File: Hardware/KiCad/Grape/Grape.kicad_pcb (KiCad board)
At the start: 2 copper layers, 68.6 x 53.3 mm, 85 parts, among them J1 USB_MICROB, J19 POWER_JACKPTH, J3 ARDUINO_R3, P1 CONN_01X03, P10 CONN_01X03, P11 CONN_01X03, P12 CONN_01X03, P13 CONN_01X03, P14 CONN_01X03, P15 CONN_01X03, P16 CONN_01X03, P17 CONN_01X03, P18 CONN_01X03, P19 CONN_01X03, P2 CONN_01X03, P20 CONN_01X03, P21 CONN_01X03, P22 CONN_01X03, P23 I2C, P3 CONN_01X03, P4 CONN_01X03, P5 CONN_01X03, P6 CONN_01X03, P7 CONN_01X03, P8 CONN_01X03, P9 CONN_01X03, Q1 2N7002PW, Q4 FDN340P, Q5 FDN340P, SW1 SW_SPDT, U1 FT231XS, U2 LM358, U3 AMS1117-3.3, U4 ATMEGA328P_TQFP, U8 MP2307SO, Y1 16MHz

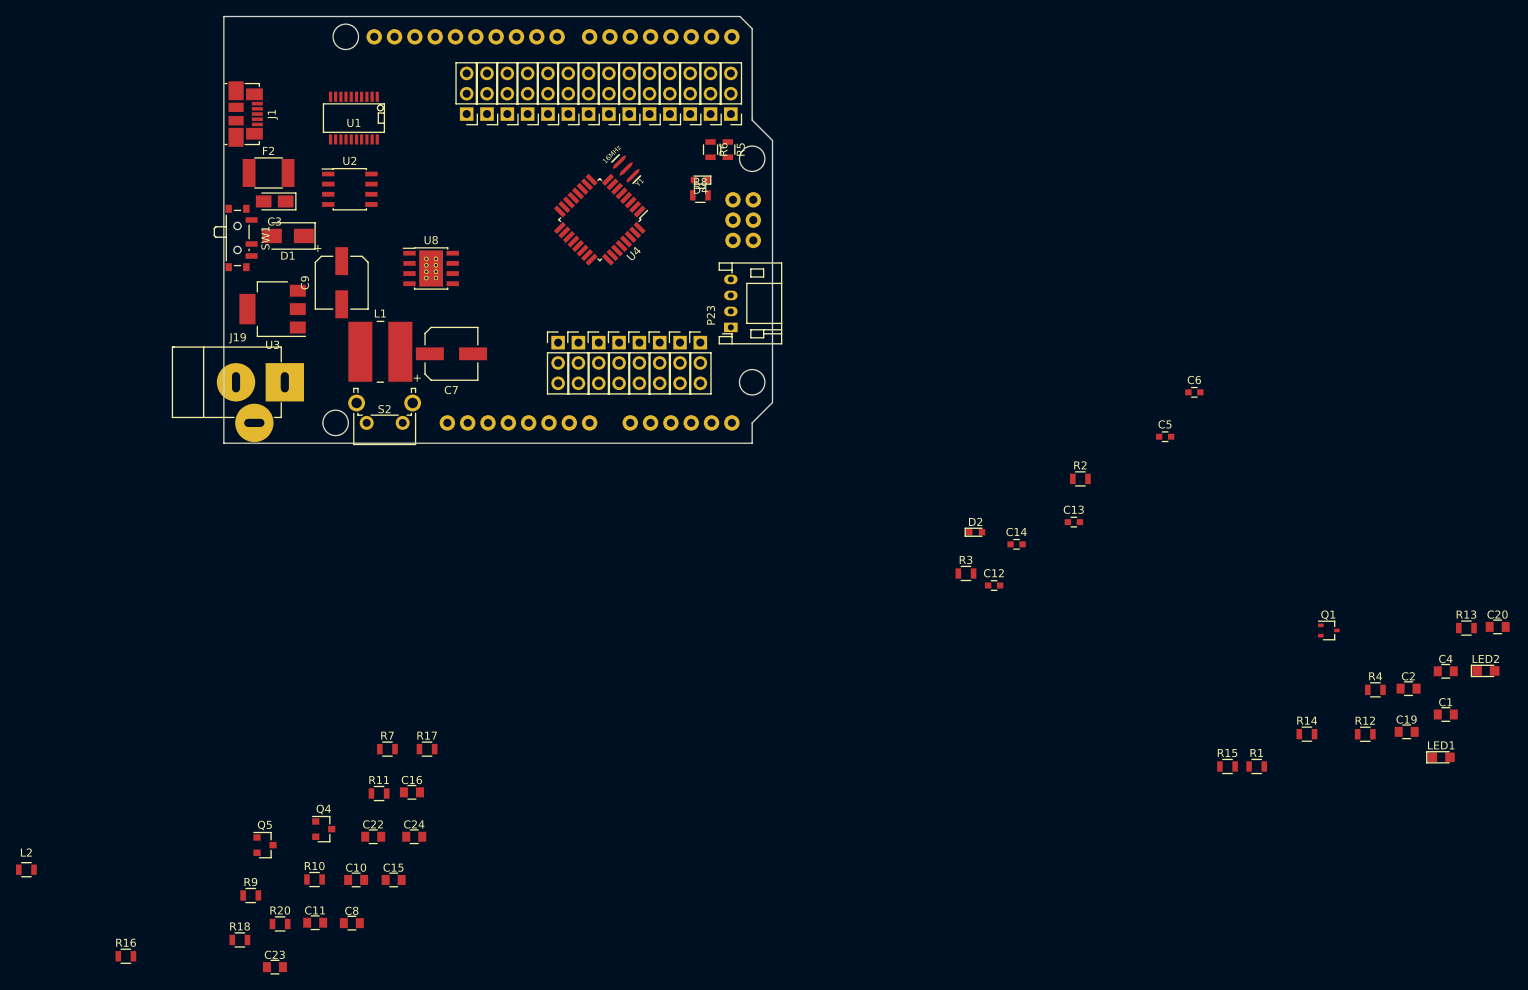
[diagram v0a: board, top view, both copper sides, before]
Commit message: 3D terminado
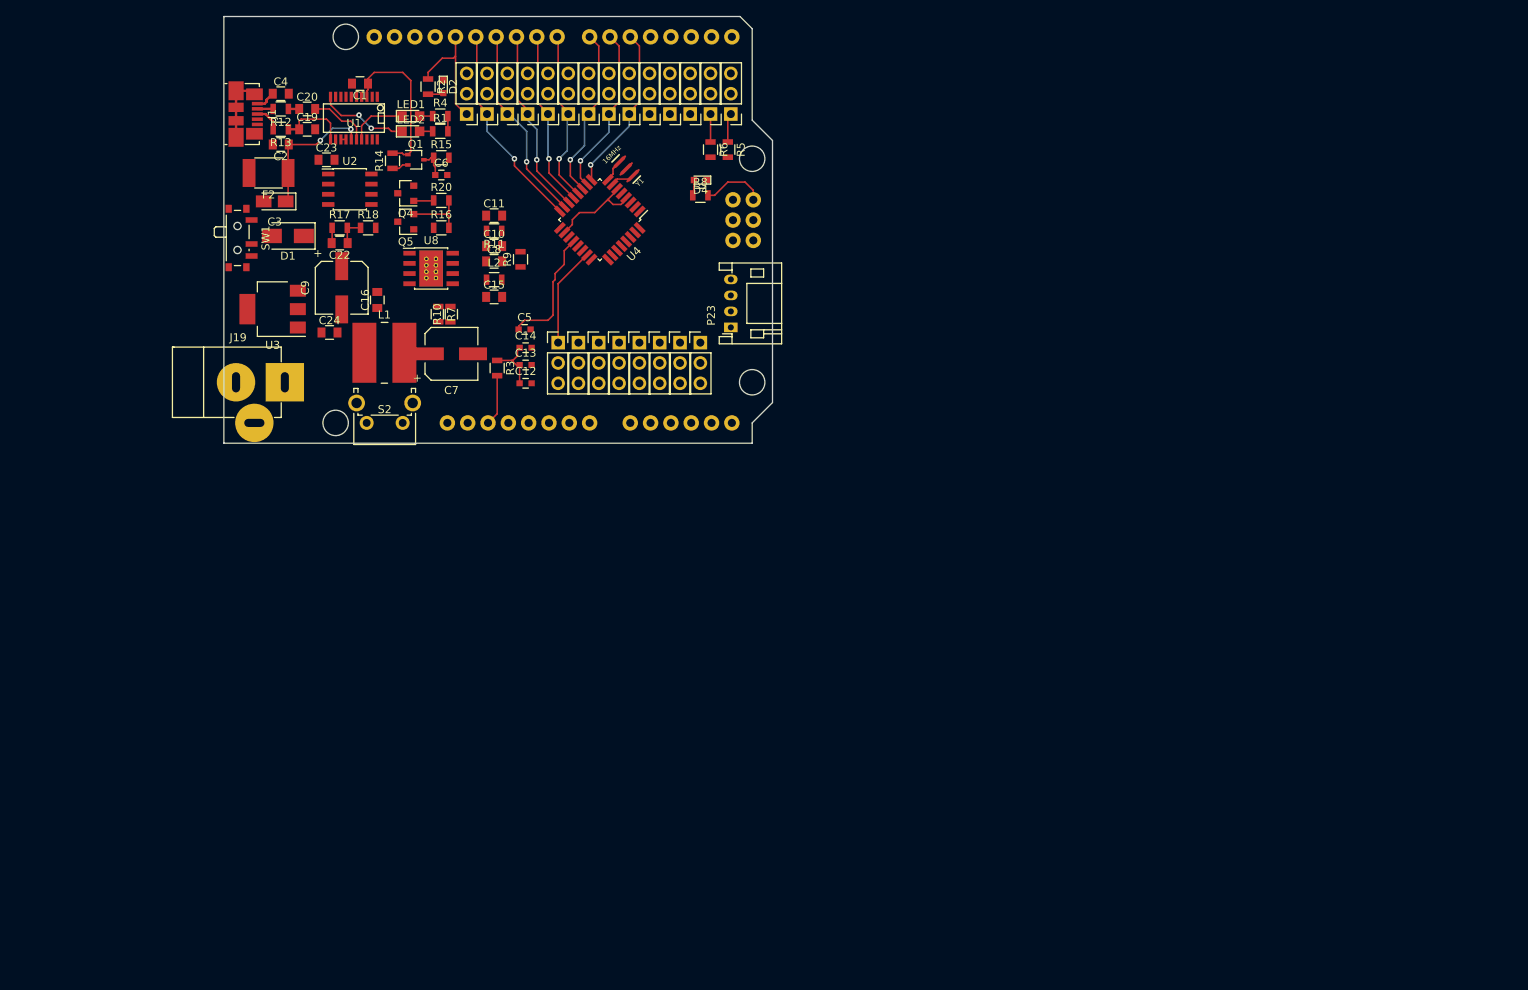
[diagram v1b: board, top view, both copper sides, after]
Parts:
- moved C4 162.5 mm to (118.9, 70.6)
- moved C20 162.3 mm to (122.2, 72.5)
- moved R13 160.8 mm to (118.9, 75.1), turned to 180 degrees
- moved C1 157.0 mm to (128.8, 69.3), turned to 180 degrees
- moved C19 156.7 mm to (122.2, 75.1)
- moved C2 156.5 mm to (118.9, 77.0), turned to 180 degrees
- moved R12 156.5 mm to (118.9, 72.5), turned to 180 degrees
- moved LED1 151.7 mm to (135.1, 73.4)
- moved LED2 150.4 mm to (135.1, 75.3)
- moved R4 137.1 mm to (138.8, 73.4)
- moved R14 134.9 mm to (132.8, 79.0), turned to 90 degrees
- moved R1 129.3 mm to (138.8, 75.3)
- moved Q1 128.4 mm to (135.8, 78.9)
- moved R15 124.3 mm to (138.9, 78.6)
- moved C23 101.1 mm to (124.6, 78.9)
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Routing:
- net +5V: track 0.00 -> 37.4 mm
- net MISO/PIN12: track 0.00 -> 26.2 mm, vias 0 -> 1
- net MOSI/PIN11: track 0.00 -> 25.0 mm, vias 0 -> 1
- net SS/PIN10: track 0.00 -> 23.5 mm, vias 0 -> 1
- net IO9/PIN9: track 0.00 -> 22.0 mm, vias 0 -> 1
- net IO8/PIN8: track 0.00 -> 21.6 mm, vias 0 -> 1
- net IO7/PIN7: track 0.00 -> 21.6 mm, vias 0 -> 1
- net IO6/PIN6: track 0.00 -> 21.3 mm, vias 0 -> 1
- net IO5/PIN5: track 0.00 -> 20.9 mm, vias 0 -> 1
- net +3V3: track 0.00 -> 20.5 mm
- net GND: track 0.00 -> 17.9 mm
- net USB_5V: track 0.00 -> 17.2 mm, vias 0 -> 2
- net AREF: track 0.00 -> 15.5 mm
- net SCK/PIN13: track 0.00 -> 15.4 mm
- net AD0: track 0.00 -> 12.5 mm
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
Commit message: Comenzado el enrutado
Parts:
- moved J19 4.10 mm to (123.4, 106.2)
- moved D1 0.28 mm to (120.0, 88.3)
- moved C7 0.25 mm to (140.5, 103.1)
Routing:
- net +5V: track 37.4 -> 139.9 mm
- net GND: track 17.9 -> 63.9 mm, vias 0 -> 2
- net AD4/SDA: track 0.00 -> 40.8 mm, vias 0 -> 2
- net RX: track 3.65 -> 39.0 mm, vias 0 -> 2
- net TX: track 3.50 -> 37.0 mm, vias 0 -> 2
- net AD5/SCL: track 0.00 -> 29.9 mm
- net Net-(J19-Pad1): track 0.00 -> 29.0 mm
- net AD3: track 0.00 -> 28.1 mm
- net AD2: track 0.00 -> 27.8 mm
- net AD1: track 0.00 -> 27.0 mm
- net AD7: track 0.00 -> 24.1 mm, vias 0 -> 1
- net AD6: track 0.00 -> 24.1 mm, vias 0 -> 1
- net Net-(C16-Pad1): track 0.00 -> 19.7 mm
- net Net-(C15-Pad1): track 0.00 -> 17.9 mm
- net AD0: track 12.5 -> 28.5 mm
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
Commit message: copia de seguridad
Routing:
- net +3V3: track 31.8 -> 109.5 mm, vias 0 -> 3
- net SCK/PIN13: track 15.4 -> 67.9 mm, vias 0 -> 2
- net GND: track 63.9 -> 111.2 mm, vias 2 -> 4
- net VDD5: track 0.00 -> 27.3 mm, vias 0 -> 2
- net Net-(Q4-Pad1): track 2.52 -> 27.8 mm, vias 0 -> 2
- net +5V: track 139.9 -> 164.6 mm
- net VIN: track 15.5 -> 38.0 mm, vias 0 -> 2
- net Net-(C4-Pad1): track 2.59 -> 20.7 mm, vias 0 -> 2
- net Net-(Q1-Pad2): track 2.10 -> 16.2 mm, vias 0 -> 2
- net Net-(R11-Pad1): track 0.00 -> 11.5 mm, vias 0 -> 2
- net AD5/SCL: track 29.9 -> 39.1 mm
- net Net-(R10-Pad2): track 1.52 -> 4.50 mm
- added copper zone on B.Cu, net GND
- added copper zone on F.Cu, net GND

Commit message: Enrutando la placa
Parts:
- moved R3 0.57 mm to (146.5, 104.9)
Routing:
- net Net-(R6-Pad2): track 0.00 -> 56.4 mm, vias 0 -> 2
- net Net-(R5-Pad2): track 0.00 -> 46.4 mm, vias 0 -> 2
- net MOSI/PIN11: track 25.0 -> 59.0 mm, vias 1 -> 3
- net RESET: track 21.0 -> 37.9 mm
- net +5V: track 164.6 -> 177.4 mm
- net Net-(C20-Pad1): track 1.35 -> 8.68 mm
- net Net-(J19-Pad1): track 29.0 -> 28.1 mm

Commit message: enrutado completo
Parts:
- added REF**: VIA-0.6mm, vias:VIA-0.6mm, F.Cu at (124.2, 87.2)
- added REF**: VIA-0.6mm, vias:VIA-0.6mm, F.Cu at (114.6, 109.5)
- added REF**: VIA-0.6mm, vias:VIA-0.6mm, F.Cu at (132.0, 109.6)
- added REF**: VIA-0.6mm, vias:VIA-0.6mm, F.Cu at (140.7, 109.2)
- added REF**: VIA-0.6mm, vias:VIA-0.6mm, F.Cu at (122.1, 70.7)
- added REF**: VIA-0.6mm, vias:VIA-0.6mm, F.Cu at (166.2, 79.9)
- added REF**: VIA-0.6mm, vias:VIA-0.6mm, F.Cu at (151.9, 100.1)
- added REF**: VIA-0.6mm, vias:VIA-0.6mm, F.Cu at (178.2, 94.7)
- added REF**: VIA-0.6mm, vias:VIA-0.6mm, F.Cu at (178.2, 99.3)
- added REF**: VIA-0.6mm, vias:VIA-0.6mm, F.Cu at (178.2, 103.0)
- moved C5 0.13 mm to (149.5, 100.1)
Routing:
- net VIN: track 38.0 -> 99.2 mm, vias 2 -> 3
- net +5V: track 177.4 -> 238.0 mm, vias 0 -> 4
- net RESET: track 37.9 -> 97.0 mm, vias 0 -> 3
- net AD5/SCL: track 39.1 -> 92.5 mm, vias 0 -> 6
- net AD4/SDA: track 40.8 -> 92.1 mm, vias 2 -> 6
- net AREF: track 15.7 -> 64.2 mm, vias 0 -> 4
- net MISO/PIN12: track 26.2 -> 59.7 mm, vias 1 -> 2
- net IO2/PIN2: track 10.7 -> 36.9 mm, vias 0 -> 1
- net GND: track 111.2 -> 128.2 mm, vias 4 -> 7
- net IO3/PIN3: track 10.7 -> 24.6 mm, vias 0 -> 1
- net IO4/PIN4: track 10.7 -> 24.1 mm, vias 0 -> 1
- net Net-(C16-Pad1): track 19.7 -> 26.2 mm
- net SCK/PIN13: track 67.9 -> 66.1 mm
- net Net-(R5-Pad2): track 46.4 -> 47.3 mm
- net Net-(R6-Pad2): track 56.4 -> 57.1 mm
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
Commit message: empezando con la serigrafia
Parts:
- added G***: LOGO, Grape:logo_grape, F.Cu at (119.9, 65.2)
- added REF**: VIA-0.6mm, vias:VIA-0.6mm, F.Cu at (134.7, 96.8)
- added REF**: VIA-0.6mm, vias:VIA-0.6mm, F.Cu at (136.4, 96.8)
- added REF**: VIA-0.6mm, vias:VIA-0.6mm, F.Cu at (144.8, 98.7)
- added REF***: OSHW-Symbol_6.7x6mm_SilkScreen, Symbols:OSHW-Symbol_6.7x6mm_SilkScreen, B.Cu at (117.0, 65.1)
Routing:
- net GND: track 128.2 -> 133.3 mm

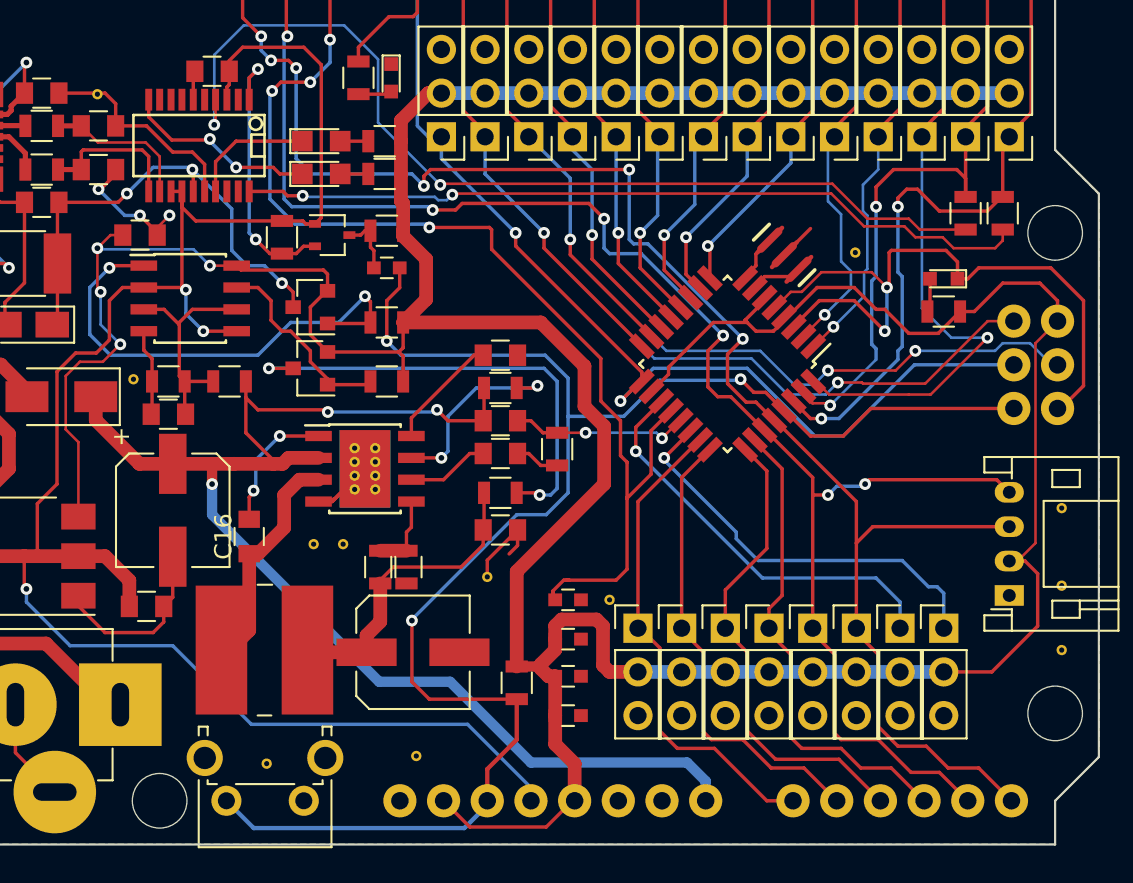
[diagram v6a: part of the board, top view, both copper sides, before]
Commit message: Avanzando con la serigrafia
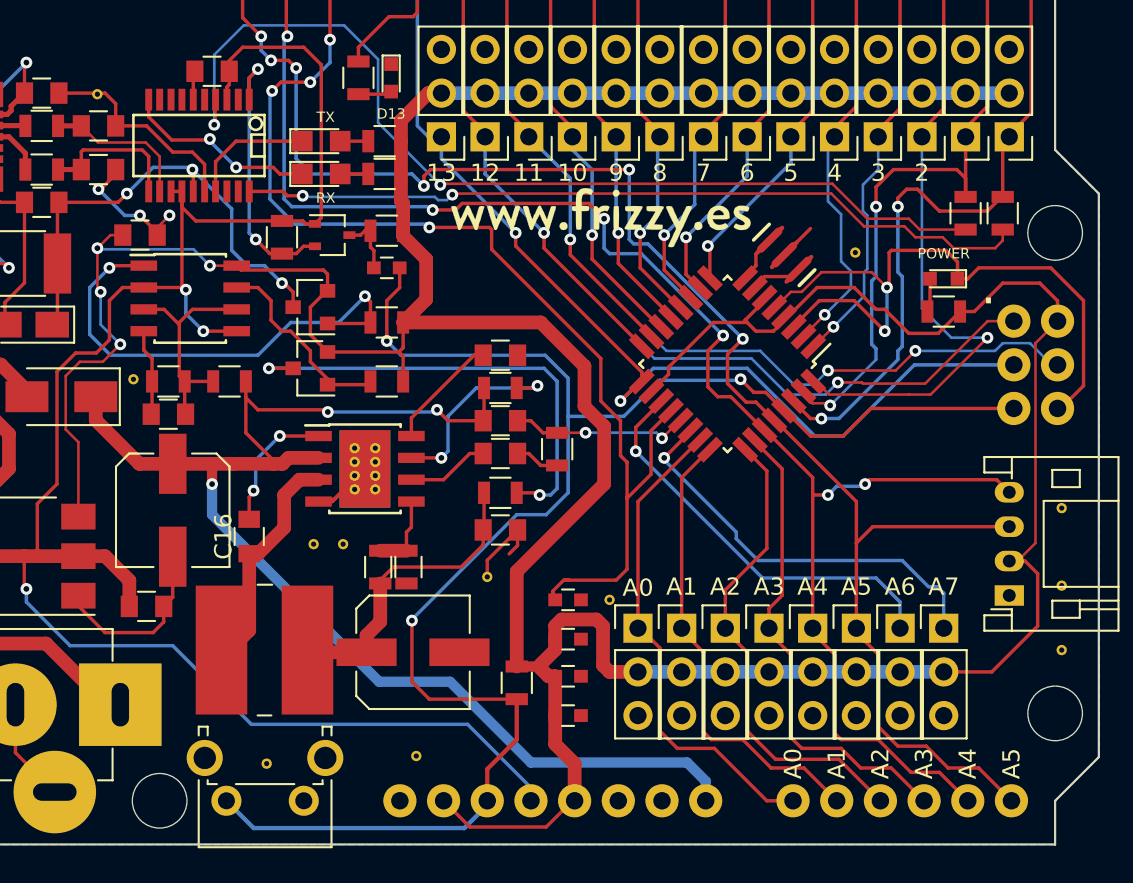
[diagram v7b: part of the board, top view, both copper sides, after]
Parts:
- added G***: LOGO, Grape:web, F.Cu at (151.4, 77.9)
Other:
- board text added: "."
- board text added: "10"
- board text added: "11"
- board text added: "12"
- board text added: "13"
- board text added: "2"
- board text added: "3"
- board text added: "4"
- board text added: "5"
- board text added: "6"
- board text added: "7"
- board text added: "8"
- board text added: "9"
- board text added: "A0"
- board text added: "A1"
- board text added: "A2"
- board text added: "A3"
- board text added: "A4"
- board text added: "A5"
- board text added: "A6"
- board text added: "A7"
- board text added: "D13"
- board text added: "DC 7 - 23V"
- board text added: "ON - OFF"
- board text added: "POWER"
- board text added: "RX"
- board text added: "TX"
